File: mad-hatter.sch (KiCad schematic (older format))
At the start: 155 parts, among them J1 XM7D-0512, J2 AVR-ISP-6, U1 ATMEGA32U4, X1 16MHz

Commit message: Various fixes:
- changes footprints to acheron
- routing fixes
- reorder ISP pins
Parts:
- removed J1: XM7D-0512, OMRON_XM7D-0512, symbol XM7D-0512:XM7D-0512
- added J1: USB_B_Mini, acheronConnectors:miniB_connector, symbol Connector:USB_B_Mini
- D_0, D_1, D_2, D_3, D_4, D_5, D_6, D_7, D_8, D_9, D_A1, D_ALT1, D_ALT2, D_B1, D_B2, D_BACKSPACE1, D_BSLSH1, D_BSLSH2, D_C1, D_CAPS_LOCK1, D_COMMA1, D_CTRL1, D_CTRL2, D_D1, D_DOT1, D_E1, D_ENTER1, D_EQUAL1, D_F1, D_G1, D_H1, D_I1, D_J1, D_K1, D_L1, D_M1, D_MINUS1, D_N1, D_O1, D_P1, D_PGDN1, D_PGUP1, D_PRSCR1, D_Q1, D_QUOTE1, D_R1, D_S1, D_SEMIC1, D_SHIFT1, D_SHIFT2, D_SLASH1, D_T1, D_TAB1, D_U1, D_V1, D_W1, D_X1, D_Y1, D_Z1, D_[1, D_]1, D_`1: footprint keyboard_parts:D_SOD123_hand -> acheronComponents:D_SOD-123
- D_FN1: renamed from D_13; footprint keyboard_parts:D_SOD123_hand -> acheronComponents:D_SOD-123
- D_GUI1: renamed from D_11; footprint keyboard_parts:D_SOD123_hand -> acheronComponents:D_SOD-123
- D_SPC1: renamed from D_10; footprint keyboard_parts:D_SOD123_hand -> acheronComponents:D_SOD-123
- D_SPC2: renamed from D_12; footprint keyboard_parts:D_SOD123_hand -> acheronComponents:D_SOD-123
- F1: value 500mA -> 1A
- K_0, K_1, K_2, K_3, K_4, K_5, K_6, K_7, K_8, K_9, K_A1, K_ALT1, K_ALT2, K_B1, K_B2, K_BACKSPACE1, K_BACKSPACE2, K_BSLSH1, K_BSLSH2, K_C1, K_CAPS_LOCK1, K_CAPS_LOCK1_2, K_COMMA1, K_CTRL1, K_CTRL2, K_D1, K_DOT1, K_E1, K_ENTER1, K_EQUAL1, K_F1, K_G1, K_H1, K_I1, K_J1, K_K1, K_L1, K_M1, K_MINUS1, K_N1, K_O1, K_P1, K_PGDN1, K_PGUP1, K_PRSCR1, K_Q1, K_QUOTE1, K_R1, K_S1, K_SEMIC1, K_SHIFT1, K_SHIFT2, K_SHIFT2_2, K_SLASH1, K_T1, K_TAB1, K_U1, K_V1, K_W1, K_X1, K_Y1, K_Z1, K_[1, K_]1, K_`1: footprint keyswitches:Kailh_socket -> acheronKeyboardSwitches:MX100H
- K_FN1: renamed from K_13; footprint keyswitches:Kailh_socket -> acheronKeyboardSwitches:MX100H
- K_GUI1: renamed from K_11; footprint keyswitches:Kailh_socket -> acheronKeyboardSwitches:MX100H
- K_GUI1_2: renamed from K_11_2; footprint keyswitches:Kailh_socket -> acheronKeyboardSwitches:MX100H
- K_SPC1: renamed from K_10; footprint keyswitches:Kailh_socket -> acheronKeyboardSwitches:MX100H
- K_SPC1_2: renamed from K_10_2; footprint keyswitches:Kailh_socket -> acheronKeyboardSwitches:MX100H
- K_SPC2: renamed from K_12; footprint keyswitches:Kailh_socket -> acheronKeyboardSwitches:MX100H
- RSW1: footprint Button_Switch_SMD:SW_SPST_TL3342 -> acheronHardware:smdPushBtn
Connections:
- net COL3: now also U1.37 (PF6); no longer U1.32 (PC7)
- net COL4: now also U1.36 (PF7); no longer U1.31 (PC6)
- net COL5: now also U1.32 (PC7); no longer U1.30 (PB6)
- net COL6: now also U1.31 (PC6); no longer U1.29 (PB5)
- net GND: now also J1.5 (GND)
- net ROW3: now also U1.30 (PB6); no longer U1.37 (PF6)
- net ROW4: now also U1.29 (PB5); no longer U1.36 (PF7)
- net VCC: now also J1.1 (VBUS)
- net at R3.2: now also J1.3 (D+)
- net at R2.2: now also J1.2 (D-)
- no-connect marks 4 -> 5

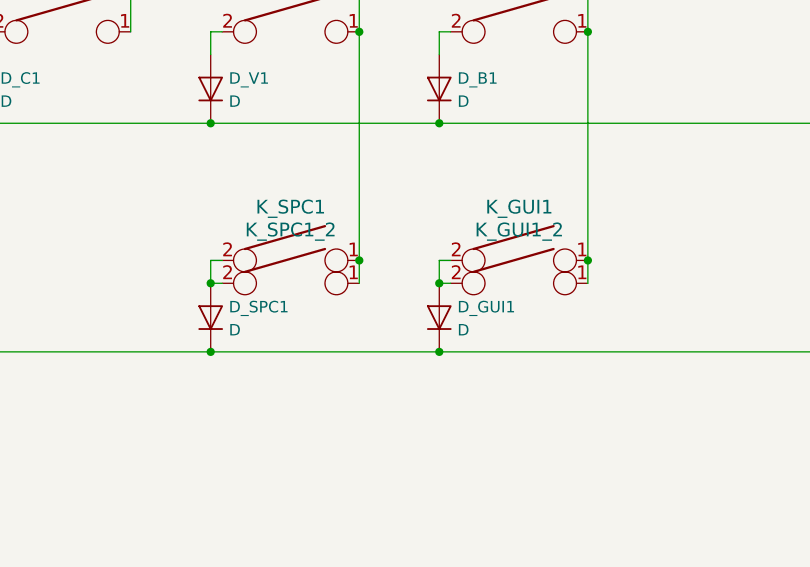
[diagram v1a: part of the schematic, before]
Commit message: Improves placement of crystal
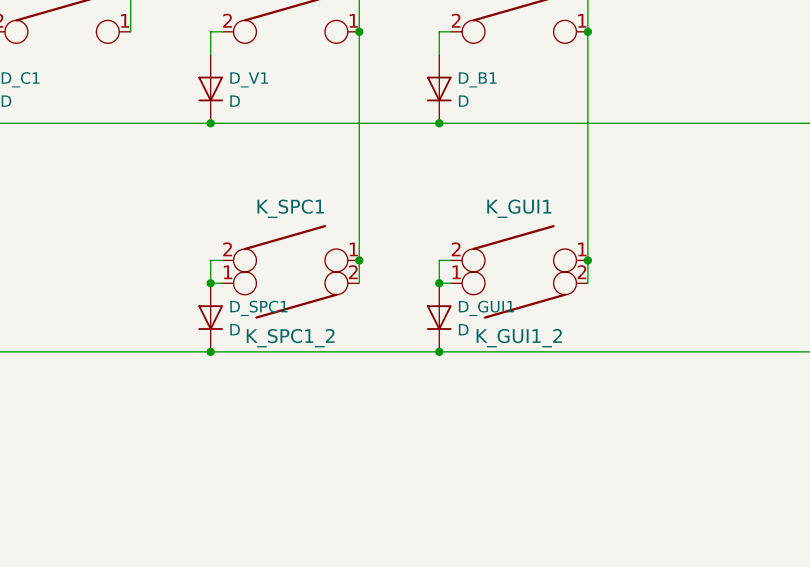
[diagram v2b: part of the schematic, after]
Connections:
- net COL5: now also K_SPC1_2.2; no longer K_SPC1_2.1
- net COL6: now also K_GUI1_2.2; no longer K_GUI1_2.1
- net at D_SPC1.2 (A), K_SPC1.2: now also K_SPC1_2.1; no longer K_SPC1_2.2
- net at D_GUI1.2 (A), K_GUI1.2: now also K_GUI1_2.1; no longer K_GUI1_2.2
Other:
- moved on the sheet: K_GUI1_2, K_SPC1_2
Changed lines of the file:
@@
 F 3 "" H 8250 6300 60  0000 C CNN
 	1    8250 6300
-	1    0    0    -1
+	-1   0    0    1
 $EndComp
 $Comp
@@
 F 3 "" H 9250 6300 60  0000 C CNN
 	1    9250 6300
-	1    0    0    -1
+	-1   0    0    1
 $EndComp
 Wire Wire Line
@@
 	3950 4300 3900 4300
 Connection ~ 3900 4300
-Wire Wire Line
-	7900 6600 8900 6600
 Connection ~ 4550 4300
 Wire Wire Line
@@
 Connection ~ 16550 4200
 Wire Wire Line
-	8900 6600 11900 6600
-Wire Wire Line
 	11550 4200 11550 5200
 Connection ~ 11550 4200
@@
 Wire Wire Line
 	2150 8900 4000 8900
+Wire Wire Line
+	7900 6600 8900 6600
+Wire Wire Line
+	8900 6600 11900 6600
 $EndSCHEMATC

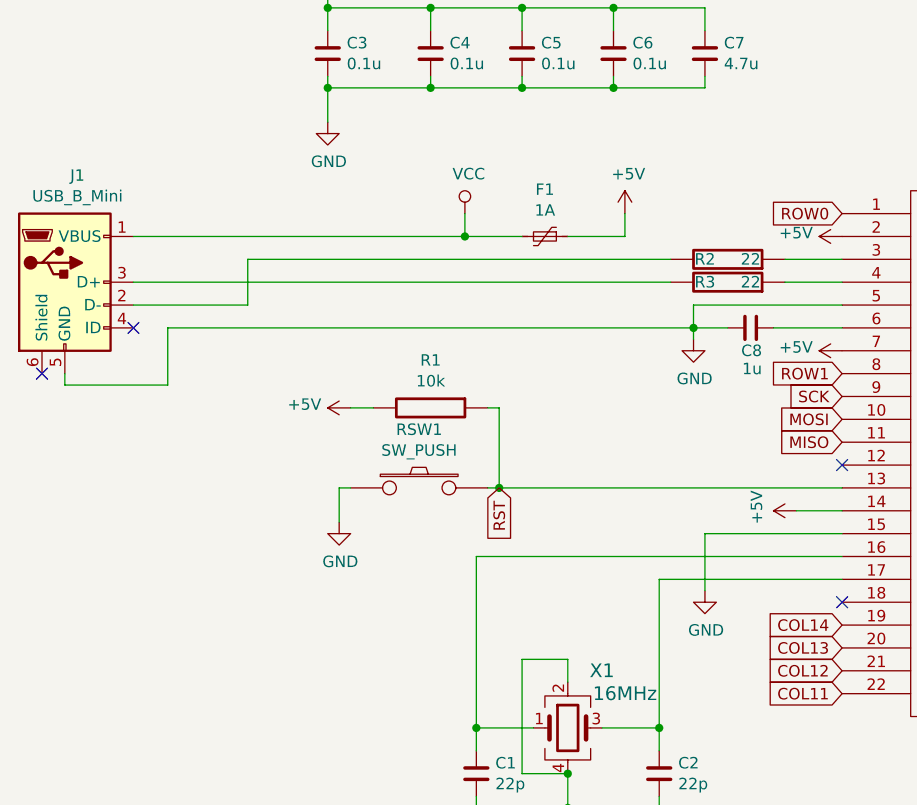
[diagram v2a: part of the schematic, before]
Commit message: Improves caps placement
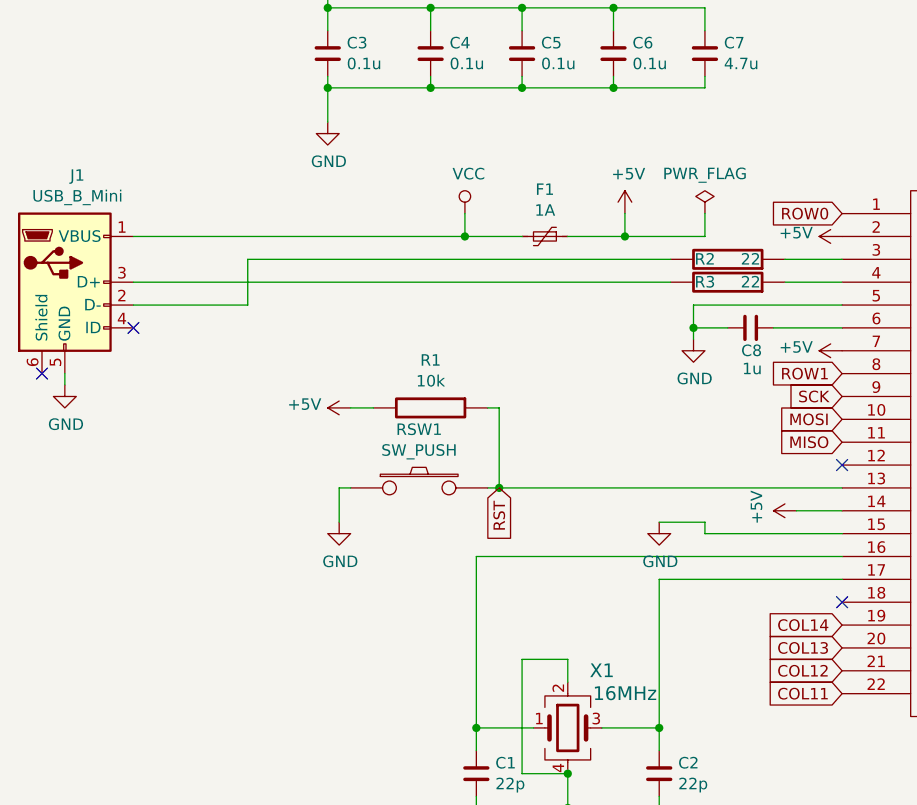
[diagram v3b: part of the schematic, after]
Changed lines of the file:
@@
 L power:GND #PWR0106
 U 1 1 5C96570D
-P 4150 10350
-F 0 "#PWR0106" H 4150 10100 50  0001 C CNN
-F 1 "GND" H 4155 10177 50  0000 C CNN
-F 2 "" H 4150 10350 50  0001 C CNN
-F 3 "" H 4150 10350 50  0001 C CNN
-	1    4150 10350
+P 3950 10050
+F 0 "#PWR0106" H 3950 9800 50  0001 C CNN
+F 1 "GND" H 3955 9877 50  0000 C CNN
+F 2 "" H 3950 10050 50  0001 C CNN
+F 3 "" H 3950 10050 50  0001 C CNN
+	1    3950 10050
 	1    0    0    -1
 $EndComp
@@
 	1    0    0    -1
 $EndComp
-Wire Wire Line
-	4150 10100 4150 10350
 Wire Wire Line
 	4150 10100 4750 10100
@@
 $EndComp
 Wire Wire Line
-	3950 11300 3950 11250
-Wire Wire Line
-	3550 11300 3950 11300
-Wire Wire Line
-	3550 11300 3550 11450
-Connection ~ 3550 11300
-Wire Wire Line
-	3150 11300 3550 11300
-Wire Wire Line
-	3150 11250 3150 11300
-Wire Wire Line
-	3550 11150 3550 11300
-Wire Wire Line
-	3950 10950 3950 11050
-Connection ~ 3950 10950
-Wire Wire Line
-	3150 10950 3150 11050
-Connection ~ 3150 10950
-$Comp
-L Device:Crystal_GND24 X1
-U 1 1 5CA386D3
-P 3550 10950
-F 0 "X1" H 3700 11200 60  0000 C CNN
-F 1 "16MHz" H 3800 11100 60  0000 C CNN
-F 2 "Crystal:Crystal_SMD_3225-4Pin_3.2x2.5mm" H 3550 10950 60  0001 C CNN
-F 3 "" H 3550 10950 60  0000 C CNN
-	1    3550 10950
-	1    0    0    -1
-$EndComp
-$Comp
-L passives:C_nonpol C2
-U 1 1 5CA2998F
-P 3950 11150
-F 0 "C2" H 4033 11196 50  0000 L CNN
-F 1 "22p" H 4033 11105 50  0000 L CNN
-F 2 "Capacitor_SMD:C_0805_2012Metric_Pad1.15x1.40mm_HandSolder" H 3988 11000 50  0001 C CNN
-F 3 "" H 3950 11150 50  0000 C CNN
-	1    3950 11150
-	1    0    0    -1
-$EndComp
-$Comp
-L passives:C_nonpol C1
-U 1 1 5CA297D7
-P 3150 11150
-F 0 "C1" H 3233 11196 50  0000 L CNN
-F 1 "22p" H 3233 11105 50  0000 L CNN
-F 2 "Capacitor_SMD:C_0805_2012Metric_Pad1.15x1.40mm_HandSolder" H 3188 11000 50  0001 C CNN
-F 3 "" H 3150 11150 50  0000 C CNN
-	1    3150 11150
-	1    0    0    -1
-$EndComp
-Wire Wire Line
 	4100 9200 4100 9250
 Wire Wire Line
-	3550 10750 3550 10650
-Wire Wire Line
-	3550 10650 3350 10650
-Wire Wire Line
-	3350 10650 3350 11150
-Wire Wire Line
-	3350 11150 3550 11150
-Connection ~ 3550 11150
-Wire Wire Line
 	4750 10200 3150 10200
 Wire Wire Line
-	3150 10200 3150 10950
-Wire Wire Line
-	3150 10950 3400 10950
-Wire Wire Line
-	3700 10950 3950 10950
-Wire Wire Line
 	3950 10300 4750 10300
-Wire Wire Line
-	3950 10300 3950 10950
 Wire Wire Line
 	3550 8800 3800 8800
@@
 	1650 9000 4000 9000
 Wire Wire Line
+	1350 9450 1350 9400
+Wire Wire Line
+	1650 9100 2150 9100
+Wire Wire Line
+	2150 9100 2150 8900
+Wire Wire Line
+	2150 8900 4000 8900
+Wire Wire Line
+	7900 6600 8900 6600
+Wire Wire Line
+	8900 6600 11900 6600
+Wire Wire Line
+	3150 11250 3150 11300
+Wire Wire Line
+	3150 11300 3550 11300
+Wire Wire Line
+	3550 11300 3550 11450
+Connection ~ 3550 11300
+Wire Wire Line
+	3550 11300 3950 11300
+Wire Wire Line
+	3950 11300 3950 11250
+$Comp
+L passives:C_nonpol C2
+U 1 1 5CA2998F
+P 3950 11150
+F 0 "C2" H 4033 11196 50  0000 L CNN
+F 1 "22p" H 4033 11105 50  0000 L CNN
+F 2 "Capacitor_SMD:C_0805_2012Metric_Pad1.15x1.40mm_HandSolder" H 3988 11000 50  0001 C CNN
+F 3 "" H 3950 11150 50  0000 C CNN
+	1    3950 11150
+	1    0    0    -1
+$EndComp
+Wire Wire Line
+	3950 10300 3950 10950
+Wire Wire Line
+	3950 10950 3950 11050
+Connection ~ 3950 10950
+Wire Wire Line
+	3700 10950 3950 10950
+Wire Wire Line
+	3150 10200 3150 10950
+Wire Wire Line
+	3150 10950 3150 11050
+Connection ~ 3150 10950
+Wire Wire Line
+	3150 10950 3400 10950
+Wire Wire Line
+	3350 11150 3550 11150
+Wire Wire Line
+	3350 10650 3350 11150
+Wire Wire Line
+	3550 10650 3350 10650
+Wire Wire Line
+	3550 10750 3550 10650
+$Comp
+L passives:C_nonpol C1
+U 1 1 5CA297D7
+P 3150 11150
+F 0 "C1" H 3233 11196 50  0000 L CNN
+F 1 "22p" H 3233 11105 50  0000 L CNN
+F 2 "Capacitor_SMD:C_0805_2012Metric_Pad1.15x1.40mm_HandSolder" H 3188 11000 50  0001 C CNN
+F 3 "" H 3150 11150 50  0000 C CNN
+	1    3150 11150
+	1    0    0    -1
+$EndComp
+$Comp
+L Device:Crystal_GND24 X1
+U 1 1 5CA386D3
+P 3550 10950
+F 0 "X1" H 3700 11200 60  0000 C CNN
+F 1 "16MHz" H 3800 11100 60  0000 C CNN
+F 2 "Crystal:Crystal_SMD_3225-4Pin_3.2x2.5mm" H 3550 10950 60  0001 C CNN
+F 3 "" H 3550 10950 60  0000 C CNN
+	1    3550 10950
+	1    0    0    -1
+$EndComp
+Connection ~ 3550 11150
+Wire Wire Line
+	3550 11150 3550 11300
+$Comp
+L power:PWR_FLAG #FLG0101
+U 1 1 5CC2AFED
+P 4150 8700
+F 0 "#FLG0101" H 4150 8775 50  0001 C CNN
+F 1 "PWR_FLAG" H 4150 8874 50  0000 C CNN
+F 2 "" H 4150 8700 50  0001 C CNN
+F 3 "~" H 4150 8700 50  0001 C CNN
+	1    4150 8700
+	1    0    0    -1
+$EndComp
+Wire Wire Line
+	4150 8700 4150 8800
+Wire Wire Line
+	4150 8800 3800 8800
+Connection ~ 3800 8800
+Wire Wire Line
 	1650 8800 3100 8800
 Wire Wire Line
-	1800 9200 1800 9450
-Wire Wire Line
-	1800 9450 1350 9450
-Wire Wire Line
-	1350 9450 1350 9400
-Wire Wire Line
-	1800 9200 4100 9200
-Wire Wire Line
-	1650 9100 2150 9100
-Wire Wire Line
-	2150 9100 2150 8900
-Wire Wire Line
-	2150 8900 4000 8900
-Wire Wire Line
-	7900 6600 8900 6600
-Wire Wire Line
-	8900 6600 11900 6600
+	4150 10100 4150 10050
+Wire Wire Line
+	3950 10050 4150 10050
+$Comp
+L power:GND #PWR?
+U 1 1 5CD01BC3
+P 1350 9450
+F 0 "#PWR?" H 1350 9200 50  0001 C CNN
+F 1 "GND" H 1355 9277 50  0000 C CNN
+F 2 "" H 1350 9450 50  0001 C CNN
+F 3 "" H 1350 9450 50  0001 C CNN
+	1    1350 9450
+	1    0    0    -1
+$EndComp
 $EndSCHEMATC
